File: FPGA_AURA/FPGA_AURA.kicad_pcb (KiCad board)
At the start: 6 copper layers, 50 x 50 mm, 129 parts, among them J100 USB_C_Receptacle_USB2.0_16P, J101 XT30PW-M, U1 XC7A35T-2FTG256C, U2 W25Q256JVEIQ, U200 ADP5014, U3 FT232HQ-REEL, U4 TPS51200DRCR, U500 MT41K128M16JT-125_IT_K

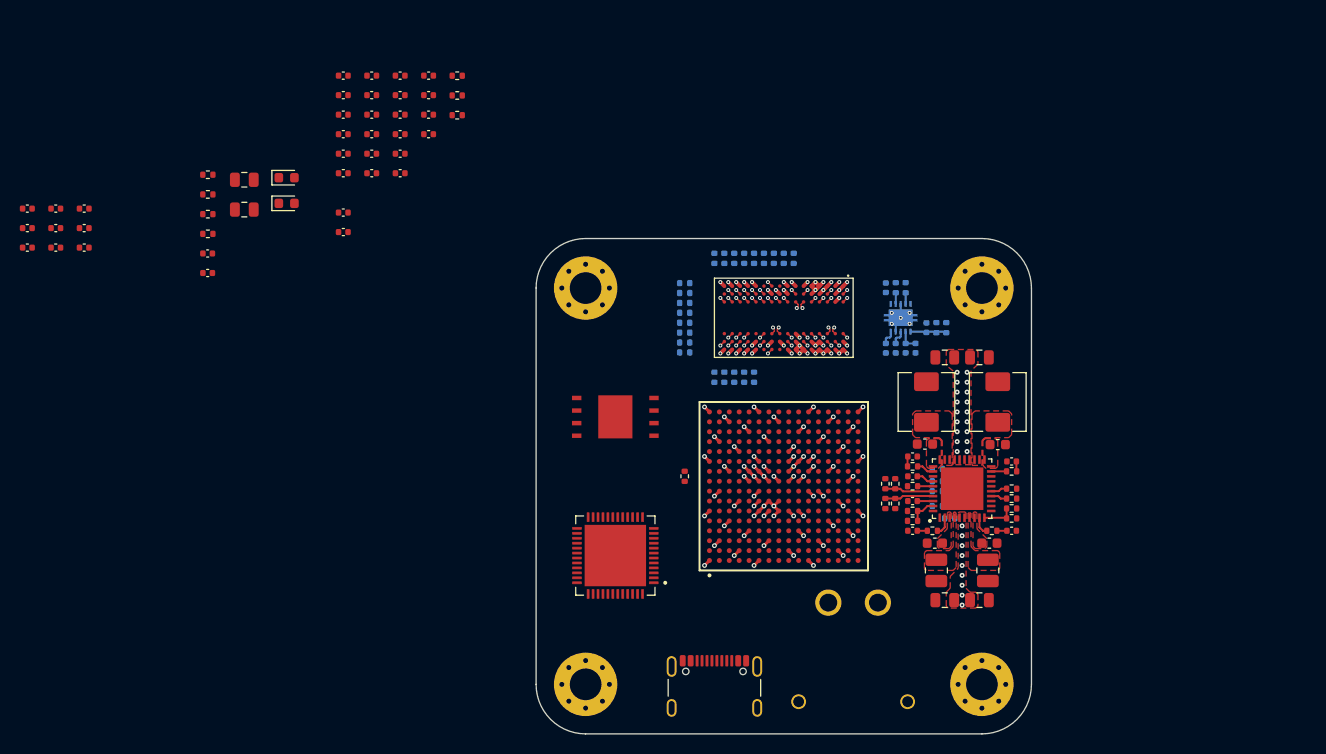
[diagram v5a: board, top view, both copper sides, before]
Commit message: Added Connectors, FPGA Power and organized sheets.
All schematic sheets now go up in order with the correct prefix.
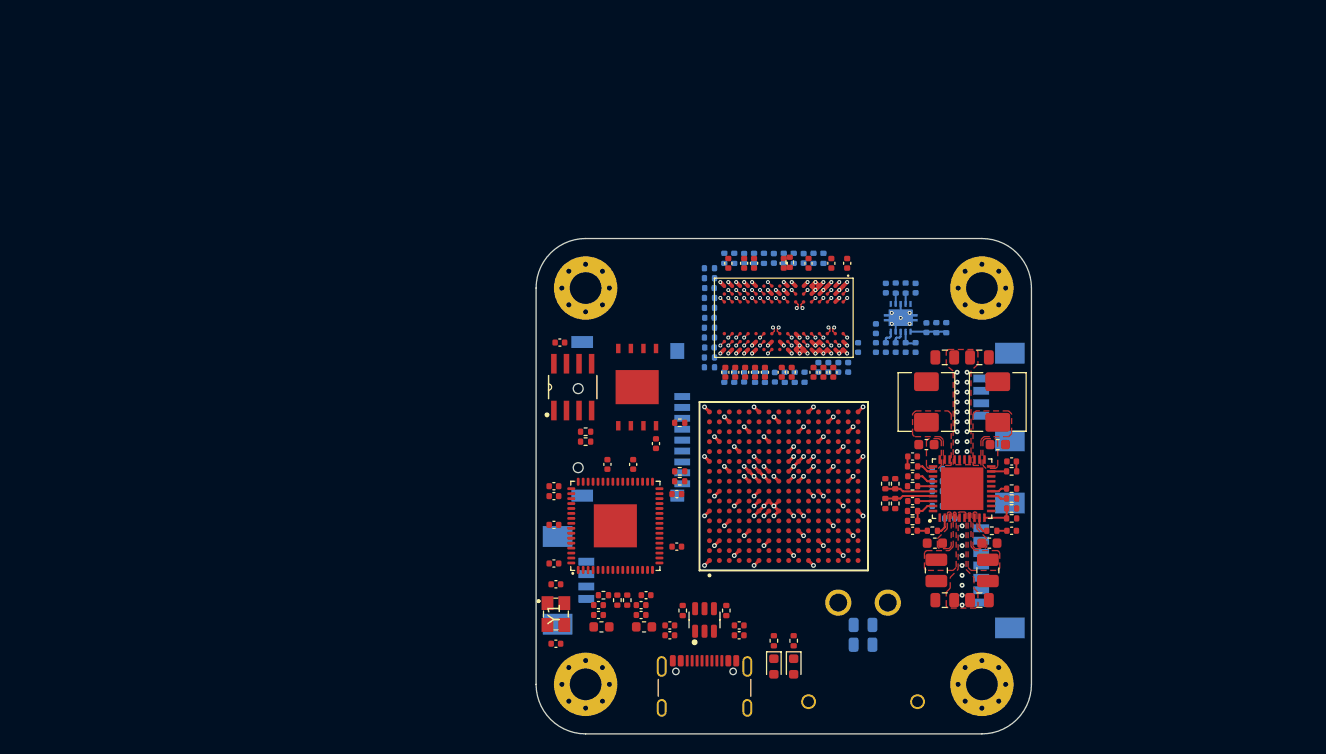
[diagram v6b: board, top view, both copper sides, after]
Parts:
- added C1: 100n, Capacitor_SMD:C_0402_1005Metric, F.Cu at (112.1, 70.7)
- added C10: 100n, Capacitor_SMD:C_0402_1005Metric, F.Cu at (109.8, 72.8)
- added C103: 100n, Capacitor_SMD:C_0402_1005Metric, F.Cu at (113.5, 90.0)
- added C105: 1u, Capacitor_SMD:C_0402_1005Metric, F.Cu at (113.5, 89.0)
- added C11: 4u7, Capacitor_SMD:C_0402_1005Metric, F.Cu at (110.6, 88.0)
- added C12: 100n, Capacitor_SMD:C_0402_1005Metric, F.Cu at (110.6, 87.0)
- added C13: 4u7, Capacitor_SMD:C_0402_1005Metric, F.Cu at (106.3, 88.0)
- added C14: 100n, Capacitor_SMD:C_0402_1005Metric, F.Cu at (106.3, 87.0)
- added C15: 27pF, Capacitor_SMD:C_0402_1005Metric, F.Cu at (102.0, 84.9)
- added C16: 27pF, Capacitor_SMD:C_0402_1005Metric, F.Cu at (102.0, 90.9)
- added C17: 100n, Capacitor_SMD:C_0402_1005Metric, F.Cu at (102.4, 60.5)
- added C2: 4u7, Capacitor_SMD:C_0402_1005Metric, F.Cu at (101.8, 75.0)
- added C3: 100n, Capacitor_SMD:C_0402_1005Metric, F.Cu at (101.8, 76.0)
- added C4: 100n, Capacitor_SMD:C_0402_1005Metric, F.Cu at (107.2, 72.8)
- added C5: 100n, Capacitor_SMD:C_0402_1005Metric, F.Cu at (114.2, 75.8)
- added C6: 100n, Capacitor_SMD:C_0402_1005Metric, F.Cu at (114.2, 81.1)
- added C7: 100n, Capacitor_SMD:C_0402_1005Metric, F.Cu at (101.8, 78.9)
- added C8: 100n, Capacitor_SMD:C_0402_1005Metric, F.Cu at (111.1, 86.0)
- added C9: 100n, Capacitor_SMD:C_0402_1005Metric, F.Cu at (101.8, 82.8)
- added FB1: 120R, Inductor_SMD:L_0603_1608Metric, F.Cu at (110.9, 89.2)
- added FB2: 120R, Inductor_SMD:L_0603_1608Metric, F.Cu at (106.6, 89.2)
- added J1: TF-CARD_H1.8, TF-CARD_H1_8:TFCARDH18, B.Cu at (107.5, 68.2)
- added J2: 532617004, 532617004:532617004, B.Cu at (105.1, 84.5)
- added J3: 532617007, 532617007:532617007, B.Cu at (144.9, 83.0)
- added J4: 532617004, 532617004:532617004, B.Cu at (144.9, 66.0)
- added R1: 10R, Resistor_SMD:R_0402_1005Metric, F.Cu at (114.5, 74.5)
- added R2: 22R, Resistor_SMD:R_0402_1005Metric, F.Cu at (109.2, 86.5)
- added R3: 22R, Resistor_SMD:R_0402_1005Metric, F.Cu at (108.2, 86.5)
- added R4: 1k, Resistor_SMD:R_0402_1005Metric, F.Cu at (105.0, 69.5)
- added R5: 12k, Resistor_SMD:R_0402_1005Metric, F.Cu at (105.0, 70.5)
- added R6: 12k, Resistor_SMD:R_0402_1005Metric, F.Cu at (106.8, 86.0)
- added U5: USBLC6-2SC6, Package_TO_SOT_SMD:SOT-23-6, F.Cu at (117.0, 88.5)
- added U6: 93LC56BT-I_SN, 93LC56BT-I_SN:SOIC127P600X175-8N, F.Cu at (103.7, 65.0)
- added Y1: 12MHz, X322512MSB4SI:X322512MSB4SI, F.Cu at (102.0, 87.9)
- C100: renamed from C223; moved to B.Cu
- C101: renamed from C224; moved to B.Cu
- C221, C222, C500, C501, C502, C503, C504, C505, C506, C507, C508, C515, C518, C520, C524, C529, R523: moved to B.Cu
- U3: value FT232HQ-REEL -> FT2232HQ; footprint FT232HQ-REEL:QFN50P800X800X90-49N -> FT2232HQ:QFN50P900X900X100-65N
- moved C508 80.3 mm to (134.3, 59.1), turned to 90 degrees
- moved C100 78.1 mm to (133.0, 91.0), turned to 180 degrees
- moved C505 75.5 mm to (127.0, 52.0), turned to -90 degrees
- moved C101 75.2 mm to (133.0, 89.0), turned to 180 degrees
- moved C500 74.3 mm to (121.0, 64.0), turned to 90 degrees
- moved C503 72.7 mm to (124.0, 52.0), turned to -90 degrees
- moved C502 72.4 mm to (121.0, 52.0), turned to -90 degrees
- moved R109 72.0 mm to (126.0, 90.6), turned to -90 degrees
- moved C506 71.8 mm to (124.1, 64.0), turned to 90 degrees
- moved R108 71.5 mm to (124.0, 90.6), turned to -90 degrees
- moved C501 69.9 mm to (117.5, 61.0)
- moved D105 69.7 mm to (124.0, 93.2), turned to -90 degrees
- moved D106 69.3 mm to (126.0, 93.2), turned to -90 degrees
- moved R100 68.4 mm to (119.2, 87.5), turned to -90 degrees
- moved C504 66.6 mm to (117.5, 58.0)
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- renumbered C225 to C102, C226 to C104
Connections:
- net /100_Power_Switching/+5V_USB renamed +5V_USB
- U1 pad E8: unconnected-(U1A-CCLK_0-PadE8) -> /400_FPGA_Config/QSPI_CLK_R
- U1 pad F8: GND -> unconnected-(U1B-VCCBATT_0-PadF8)
- U1 pad G7: GND -> unconnected-(U1B-GNDADC_0-PadG7)
- U1 pad H7: GND -> unconnected-(U1B-VREFN_0-PadH7)
- U1 pad J13: unconnected-(U1A-IO_L1P_T0_D00_MOSI_14-PadJ13) -> /400_FPGA_Config/QSPI_IO0
- U1 pad J14: unconnected-(U1A-IO_L1N_T0_D01_DIN_14-PadJ14) -> /400_FPGA_Config/QSPI_IO1
- U1 pad K15: unconnected-(U1A-IO_L2P_T0_D02_14-PadK15) -> /400_FPGA_Config/QSPI_IO2
- U1 pad K16: unconnected-(U1A-IO_L2N_T0_D03_14-PadK16) -> /400_FPGA_Config/QSPI_IO3
- U1 pad L12: unconnected-(U1A-IO_L6P_T0_FCS_B_14-PadL12) -> /400_FPGA_Config/QSPI_CS#
- U1 pad L6: unconnected-(U1A-VCCO_0-PadL6) -> +3V3
- U2 pad 1: unconnected-(U2-/CS-Pad1) -> /400_FPGA_Config/QSPI_CS#
- U2 pad 2: unconnected-(U2-DO_(IO1)_1-Pad2) -> /400_FPGA_Config/QSPI_IO1
- U2 pad 3: unconnected-(U2-DO_(IO1)_2-Pad3) -> /400_FPGA_Config/QSPI_IO2
- U2 pad 4: unconnected-(U2-GND-Pad4) -> GND
- U2 pad 5: unconnected-(U2-DI_(IO0)-Pad5) -> /400_FPGA_Config/QSPI_IO0
- U2 pad 6: unconnected-(U2-CLK-Pad6) -> /400_FPGA_Config/QSPI_CLK
- U2 pad 7: unconnected-(U2-/HOLD-Pad7) -> /400_FPGA_Config/QSPI_IO3
- U2 pad 8: unconnected-(U2-VCC-Pad8) -> +3V3
- U2 pad 9: unconnected-(U2-/WP-Pad9) -> GND
- U3 pad 1: unconnected-(U3-OSCI-Pad1) -> GND
- U3 pad 12: unconnected-(U3-VCCIO-Pad12) -> +1V8_FTDI
- U3 pad 13: unconnected-(U3-ADBUS0-Pad13) -> GND
- U3 pad 15: unconnected-(U3-ADBUS2-Pad15) -> GND
- U3 pad 2: unconnected-(U3-OSCO-Pad2) -> /400_FPGA_Config/OSCI_FTDI
- U3 pad 20: unconnected-(U3-ADBUS7-Pad20) -> +3V3
- U3 pad 22: GND -> unconnected-(U3-ADBUS5-Pad22)
- U3 pad 23: GND -> unconnected-(U3-ADBUS6-Pad23)
- U3 pad 25: unconnected-(U3-ACBUS1-Pad25) -> GND
- U3 pad 3: unconnected-(U3-VPHY-Pad3) -> /400_FPGA_Config/OSCO_FTDI
- U3 pad 31: unconnected-(U3-ACBUS7-Pad31) -> +3V3
- U3 pad 36: GND -> unconnected-(U3-~{SUSPEND}#-Pad36)
- U3 pad 37: unconnected-(U3-VCCA-Pad37) -> +1V8_FTDI
- U3 pad 4: GND -> /400_FPGA_Config/VPHY_FTDI
- U3 pad 41: GND -> unconnected-(U3-BDBUS3-Pad41)
- U3 pad 42: unconnected-(U3-TEST-Pad42) -> +3V3
- U3 pad 48: GND -> unconnected-(U3-BCBUS0-Pad48)
- U3 pad 49: GND -> +1V8_FTDI
- U3 pad 5: unconnected-(U3-REF-Pad5) -> GND
- U3 pad 6: unconnected-(U3-DM-Pad6) -> /400_FPGA_Config/FTDI_REF
- U3 pad 7: unconnected-(U3-DP-Pad7) -> /400_FPGA_Config/USB_R_D-
- U3 pad 8: unconnected-(U3-VPLL-Pad8) -> /400_FPGA_Config/USB_R_D+
- U3 pad 9: GND -> /400_FPGA_Config/VPLL_FTDI
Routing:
- net unconnected-(U1B-VCCBATT_0-PadF8): track 0.00 -> 0.71 mm, vias 0 -> 1
- net GND: track 50.1 -> 49.4 mm, vias 86 -> 85

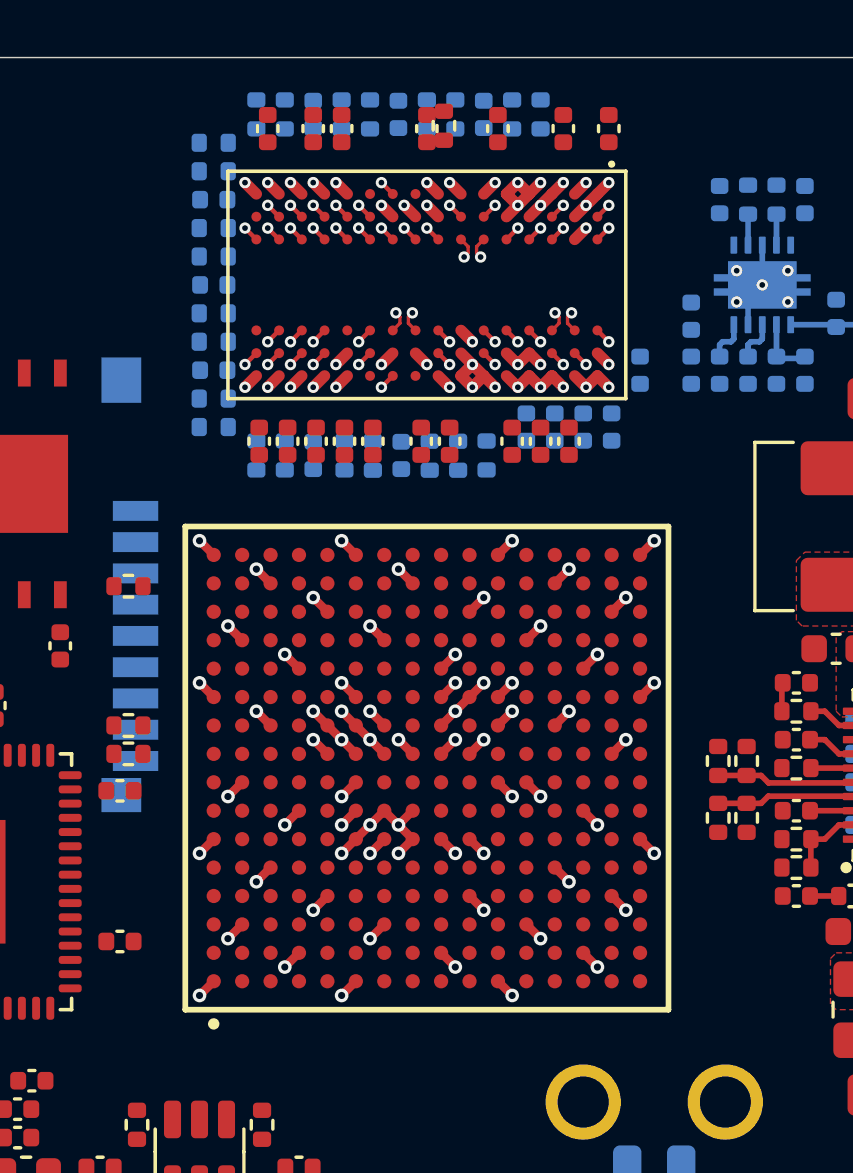
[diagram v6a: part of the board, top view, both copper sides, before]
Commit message: Following new DDR3 reference
Using Scopefun v2 as a reference design for the XC7A35T-FTG256
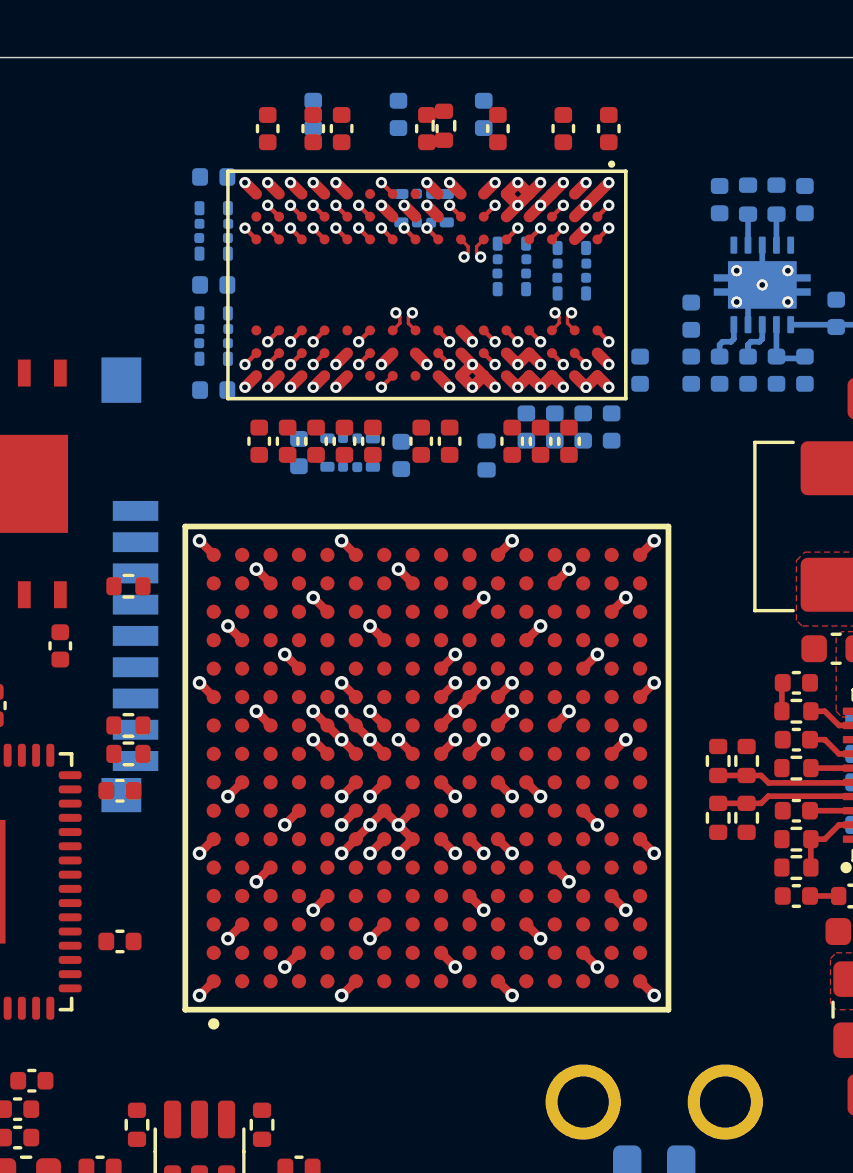
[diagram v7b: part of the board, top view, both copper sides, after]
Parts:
- removed R500, R501, R502, R503, R504, R505, R506, R507, R514, R515, R516, R517, R518, R519, R520, R521: 40R2, Resistor_SMD:R_0402_1005Metric
- R508, R509, R510, R511, R512, R513: value 40R2 -> ~; footprint Resistor_SMD:R_0402_1005Metric -> YC124-FR-0740R2L:0402_4
- R523: value 240 -> 240R
- moved R510 9.79 mm to (130.1, 57.5), turned to 0 degrees
- moved R509 8.26 mm to (128.0, 57.3), turned to 0 degrees
- moved R508 8.19 mm to (117.5, 59.8), turned to 0 degrees
- moved R512 4.88 mm to (122.3, 63.9), turned to 90 degrees
- moved R513 3.81 mm to (124.9, 55.3)
- moved C507 0.80 mm to (117.5, 54.2)
- moved C501 0.70 mm to (117.5, 61.7)
- moved C500 0.51 mm to (120.5, 63.9)
- moved R511 0.10 mm to (117.5, 56.1)
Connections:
- R508 pad 1: +VTT -> unconnected-(R508-Pad1)
- R508 pad 2: DDR3_A5 -> DDR3_A7
- R509 pad 2: DDR3_A4 -> DDR3_A3
- R510 pad 2: DDR3_A3 -> DDR3_BA0
- R511 pad 2: DDR3_A2 -> DDR3_CS
- R512 pad 2: DDR3_A1 -> DDR3_A11
- R513 pad 1: +VTT -> unconnected-(R513-Pad1)
- R513 pad 2: DDR3_A0 -> unconnected-(R513-Pad2)
- U1 pad A10: unconnected-(U1D-IO_L3N_T0_DQS_AD1N_15-PadA10) -> DDR3_CK-
- U1 pad A12: unconnected-(U1D-IO_L5N_T0_AD9N_15-PadA12) -> DDR3_A6
- U1 pad A13: unconnected-(U1D-IO_L7P_T1_AD2P_15-PadA13) -> DDR3_A14
- U1 pad A14: unconnected-(U1D-IO_L7N_T1_AD2N_15-PadA14) -> DDR3_BA2
- U1 pad A15: unconnected-(U1D-IO_L9N_T1_DQS_AD3N_15-PadA15) -> DDR3_A13
- U1 pad A8: unconnected-(U1D-IO_L2P_T0_AD8P_15-PadA8) -> DDR3_CKE
- U1 pad A9: unconnected-(U1D-IO_L2N_T0_AD8N_15-PadA9) -> DDR3_A4
- U1 pad B10: unconnected-(U1D-IO_L4P_T0_15-PadB10) -> DDR3_CAS
- U1 pad B11: unconnected-(U1D-IO_L4N_T0_15-PadB11) -> DDR3_BA1
- U1 pad B12: unconnected-(U1D-IO_L5P_T0_AD9P_15-PadB12) -> DDR3_A8
- U1 pad B14: unconnected-(U1D-IO_L8N_T1_AD10N_15-PadB14) -> DDR3_A1
- U1 pad B15: unconnected-(U1D-IO_L9P_T1_DQS_AD3P_15-PadB15) -> DDR3_A0
- U1 pad B16: unconnected-(U1D-IO_L10N_T1_AD11N_15-PadB16) -> DDR3_WE
- U1 pad B9: unconnected-(U1D-IO_L3P_T0_DQS_AD1P_15-PadB9) -> DDR3_CK+
- U1 pad C11: unconnected-(U1D-IO_L11P_T1_SRCC_15-PadC11) -> DDR3_BA0
- U1 pad C12: unconnected-(U1D-IO_L11N_T1_SRCC_15-PadC12) -> DDR3_A12
- U1 pad C13: unconnected-(U1D-IO_L12N_T1_MRCC_15-PadC13) -> DDR3_A11
- U1 pad C14: unconnected-(U1D-IO_L8P_T1_AD10P_15-PadC14) -> DDR3_A9
- U1 pad C16: unconnected-(U1D-IO_L10P_T1_AD11P_15-PadC16) -> DDR3_A7
- U1 pad C8: unconnected-(U1D-IO_L1P_T0_AD0P_15-PadC8) -> DDR3_A10
- U1 pad C9: unconnected-(U1D-IO_L1N_T0_AD0N_15-PadC9) -> DDR3_ODT
- U1 pad D10: unconnected-(U1D-IO_0_15-PadD10) -> DDR3_A2
- U1 pad D11: unconnected-(U1D-IO_L14N_T2_SRCC_15-PadD11) -> DDR3_DQ10
- U1 pad D13: unconnected-(U1D-IO_L12P_T1_MRCC_15-PadD13) -> DDR3_A3
- U1 pad D14: unconnected-(U1D-IO_L15P_T2_DQS_15-PadD14) -> DDR3_DQS1+
- U1 pad D15: unconnected-(U1D-IO_L15N_T2_DQS_ADV_B_15-PadD15) -> DDR3_DQS1-
- U1 pad D16: unconnected-(U1D-IO_L17N_T2_A25_15-PadD16) -> DDR3_DQ9
- U1 pad D8: unconnected-(U1D-IO_L6P_T0_15-PadD8) -> DDR3_RAS
- U1 pad D9: unconnected-(U1D-IO_L6N_T0_VREF_15-PadD9) -> DDR3_A5
- U1 pad E11: unconnected-(U1D-IO_L14P_T2_SRCC_15-PadE11) -> DDR3_DQ14
- U1 pad E12: unconnected-(U1D-IO_L13P_T2_MRCC_15-PadE12) -> DDR3_RESET
- U1 pad E15: unconnected-(U1D-IO_L18N_T2_A23_15-PadE15) -> DDR3_DQ8
- U1 pad E16: unconnected-(U1D-IO_L17P_T2_A26_15-PadE16) -> DDR3_DQ15
- U1 pad F12: unconnected-(U1D-IO_L16P_T2_A28_15-PadF12) -> DDR3_DQ12
- U1 pad F13: unconnected-(U1D-IO_L16N_T2_A27_15-PadF13) -> DDR3_DQ11
- U1 pad F14: unconnected-(U1D-IO_L21N_T3_DQS_A18_15-PadF14) -> DDR3_DQS0-
- U1 pad F15: unconnected-(U1D-IO_L18P_T2_A24_15-PadF15) -> DDR3_DQ13
- U1 pad F8: unconnected-(U1B-VCCBATT_0-PadF8) -> GND
- U1 pad G12: unconnected-(U1D-IO_L19N_T3_A21_VREF_15-PadG12) -> DDR3_DQ1
- U1 pad G14: unconnected-(U1D-IO_L21P_T3_DQS_15-PadG14) -> DDR3_DQS0+
- U1 pad G16: unconnected-(U1D-IO_L22N_T3_A16_15-PadG16) -> DDR3_DQ3
- U1 pad G7: unconnected-(U1B-GNDADC_0-PadG7) -> GND
- U1 pad G8: unconnected-(U1B-VCCADC_0-PadG8) -> +1V8
- U1 pad H11: unconnected-(U1D-IO_L19P_T3_A22_15-PadH11) -> DDR3_DQ0
- U1 pad H12: unconnected-(U1D-IO_L20P_T3_A20_15-PadH12) -> DDR3_DQ2
- U1 pad H13: unconnected-(U1D-IO_L20N_T3_A19_15-PadH13) -> DDR3_DQ6
- U1 pad H16: unconnected-(U1D-IO_L22P_T3_A17_15-PadH16) -> DDR3_DQ7
- U1 pad H7: unconnected-(U1B-VREFN_0-PadH7) -> GND
- U1 pad J15: unconnected-(U1D-IO_L23P_T3_FOE_B_15-PadJ15) -> DDR3_DQ4
- U1 pad J16: unconnected-(U1D-IO_L23N_T3_FWE_B_15-PadJ16) -> DDR3_DQ5
- U1 pad J8: unconnected-(U1B-VREFP_0-PadJ8) -> GND
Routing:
- net GND: track 49.4 -> 50.8 mm, vias 85 -> 87
- net +3V3: track 9.90 -> 11.3 mm, vias 14 -> 16
- net unconnected-(U1B-VCCBATT_0-PadF8): track 0.71 -> 0.00 mm, vias 1 -> 0
- net +1V8: track 3.54 -> 4.24 mm, vias 4 -> 5

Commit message: Moving to laptop
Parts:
- moved R510 8.98 mm to (123.8, 63.9), turned to 90 degrees
- moved R509 6.79 mm to (123.8, 52.0), turned to -90 degrees
- moved R513 5.91 mm to (120.0, 52.0)
- moved C502 2.90 mm to (118.1, 52.0)
- moved C500 2.40 mm to (118.1, 63.9)
- moved R512 2.30 mm to (120.0, 63.9)
- moved C506 2.20 mm to (121.9, 63.9)
- moved C503 2.10 mm to (121.9, 52.0)
- moved C505 1.30 mm to (125.7, 52.0)
- moved R523 1.08 mm to (127.5, 63.0)
- moved C501 1.00 mm to (116.5, 61.7)
- moved C504 1.00 mm to (116.5, 58.0)
- moved C507 1.00 mm to (116.5, 54.2)
- moved R508 1.00 mm to (116.5, 59.8)
- moved R511 1.00 mm to (116.5, 56.1)
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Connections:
- R508 pad 1: unconnected-(R508-Pad1) -> +VTT
- R508 pad 3: unconnected-(R508-Pad3) -> +VTT
- R508 pad 5: unconnected-(R508-Pad5) -> +VTT
- R508 pad 7: unconnected-(R508-Pad7) -> +VTT
- U1 pad A12: DDR3_A6 -> DDR3_A11
- U1 pad A13: DDR3_A14 -> DDR3_A1
- U1 pad A14: DDR3_BA2 -> DDR3_A8
- U1 pad A15: DDR3_A13 -> DDR3_A6
- U1 pad A8: DDR3_CKE -> DDR3_BA2
- U1 pad A9: DDR3_A4 -> DDR3_WE
- U1 pad B10: DDR3_CAS -> DDR3_A10
- U1 pad B11: DDR3_BA1 -> DDR3_A12
- U1 pad B12: DDR3_A8 -> DDR3_A4
- U1 pad B14: DDR3_A1 -> unconnected-(U1D-IO_L8N_T1_AD10N_15-PadB14)
- U1 pad B15: DDR3_A0 -> DDR3_CAS
- U1 pad B16: DDR3_WE -> DDR3_BA1
- U1 pad C11: DDR3_BA0 -> DDR3_A2
- U1 pad C12: DDR3_A12 -> DDR3_A3
- U1 pad C13: DDR3_A11 -> DDR3_ODT
- U1 pad C14: DDR3_A9 -> DDR3_RAS
- U1 pad C16: DDR3_A7 -> DDR3_CKE
- U1 pad C8: DDR3_A10 -> DDR3_A0
- U1 pad C9: DDR3_ODT -> DDR3_A7
- U1 pad D10: DDR3_A2 -> DDR3_A5
- U1 pad D13: DDR3_A3 -> DDR3_BA0
- U1 pad D8: DDR3_RAS -> DDR3_A13
- U1 pad D9: DDR3_A5 -> DDR3_A9
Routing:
- net DDR3_A7: track 0.57 -> 61.2 mm, vias 1 -> 2
- net DDR3_A5: track 0.57 -> 60.2 mm, vias 1 -> 2
- net DDR3_A2: track 0.57 -> 57.0 mm, vias 1 -> 2
- net DDR3_A9: track 0.57 -> 52.8 mm, vias 1 -> 2
- net DDR3_A3: track 0.57 -> 51.1 mm, vias 1 -> 2
- net DDR3_A13: track 0.57 -> 44.6 mm, vias 1 -> 2
- net DDR3_BA0: track 0.57 -> 44.4 mm, vias 1 -> 2
- net DDR3_A0: track 0.57 -> 40.9 mm, vias 1 -> 2
- net DDR3_ODT: track 0.57 -> 38.6 mm, vias 1 -> 2
- net DDR3_BA2: track 0.57 -> 36.5 mm, vias 1 -> 2
- net DDR3_CK+: track 0.78 -> 34.6 mm, vias 1 -> 2
- net DDR3_WE: track 0.57 -> 34.3 mm, vias 1 -> 2
- net DDR3_CK-: track 0.78 -> 32.1 mm, vias 1 -> 2
- net DDR3_A10: track 0.57 -> 28.0 mm, vias 1 -> 2
- net DDR3_RAS: track 0.57 -> 23.4 mm, vias 1 -> 2
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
